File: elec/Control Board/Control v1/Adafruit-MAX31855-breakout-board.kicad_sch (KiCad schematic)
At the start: 17 parts, among them IC1 MAX6675, IC2 LP298XS, J1 1X2-3.5MM

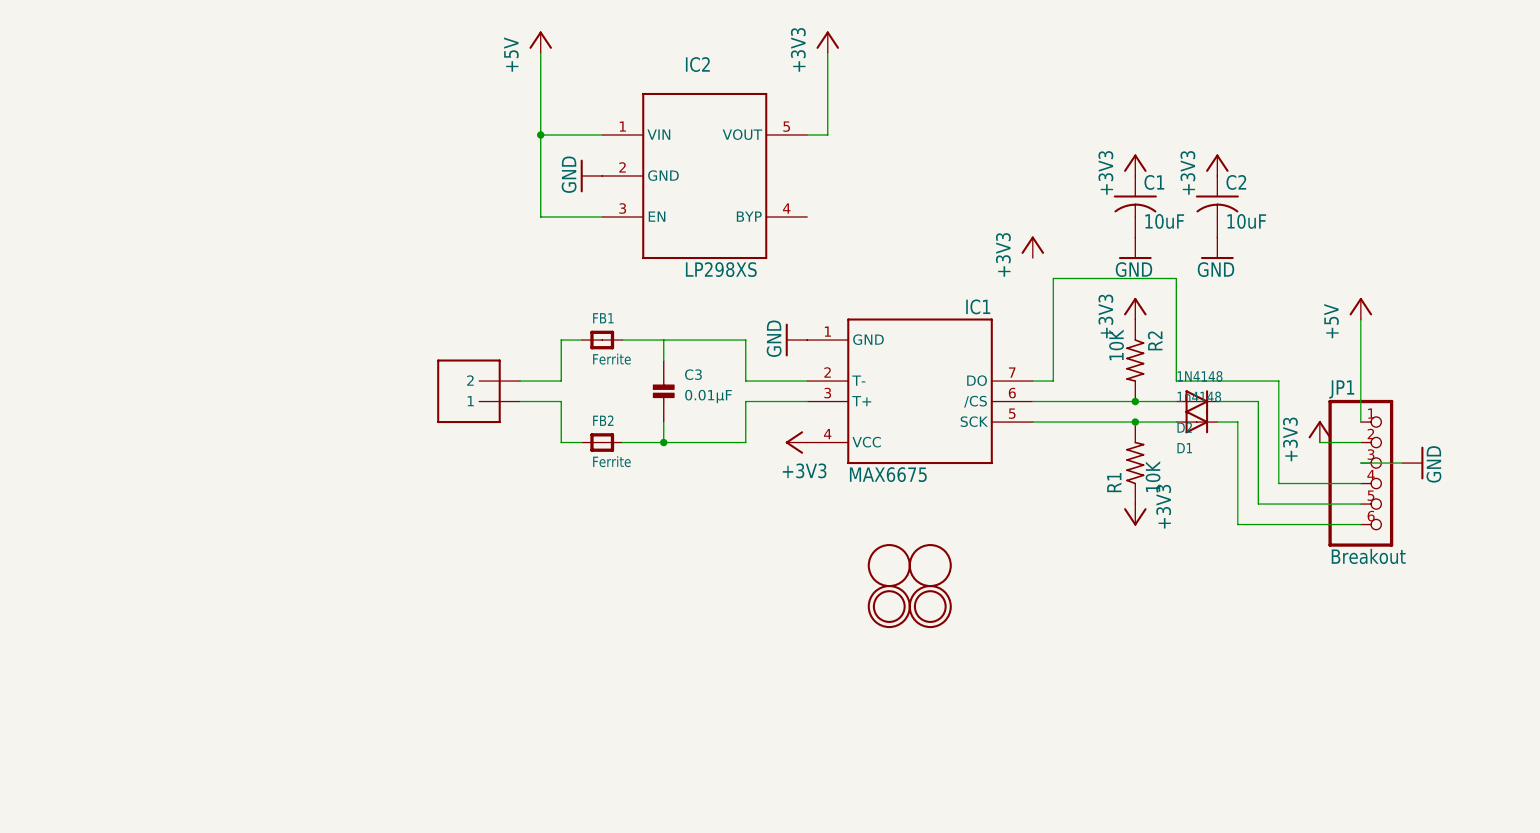
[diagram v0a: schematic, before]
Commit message: added labels for heiarchy sheets, and first pass on basic control interface circuits
Signed-off-by: lokimetasmith <lokimail@gmail.com>
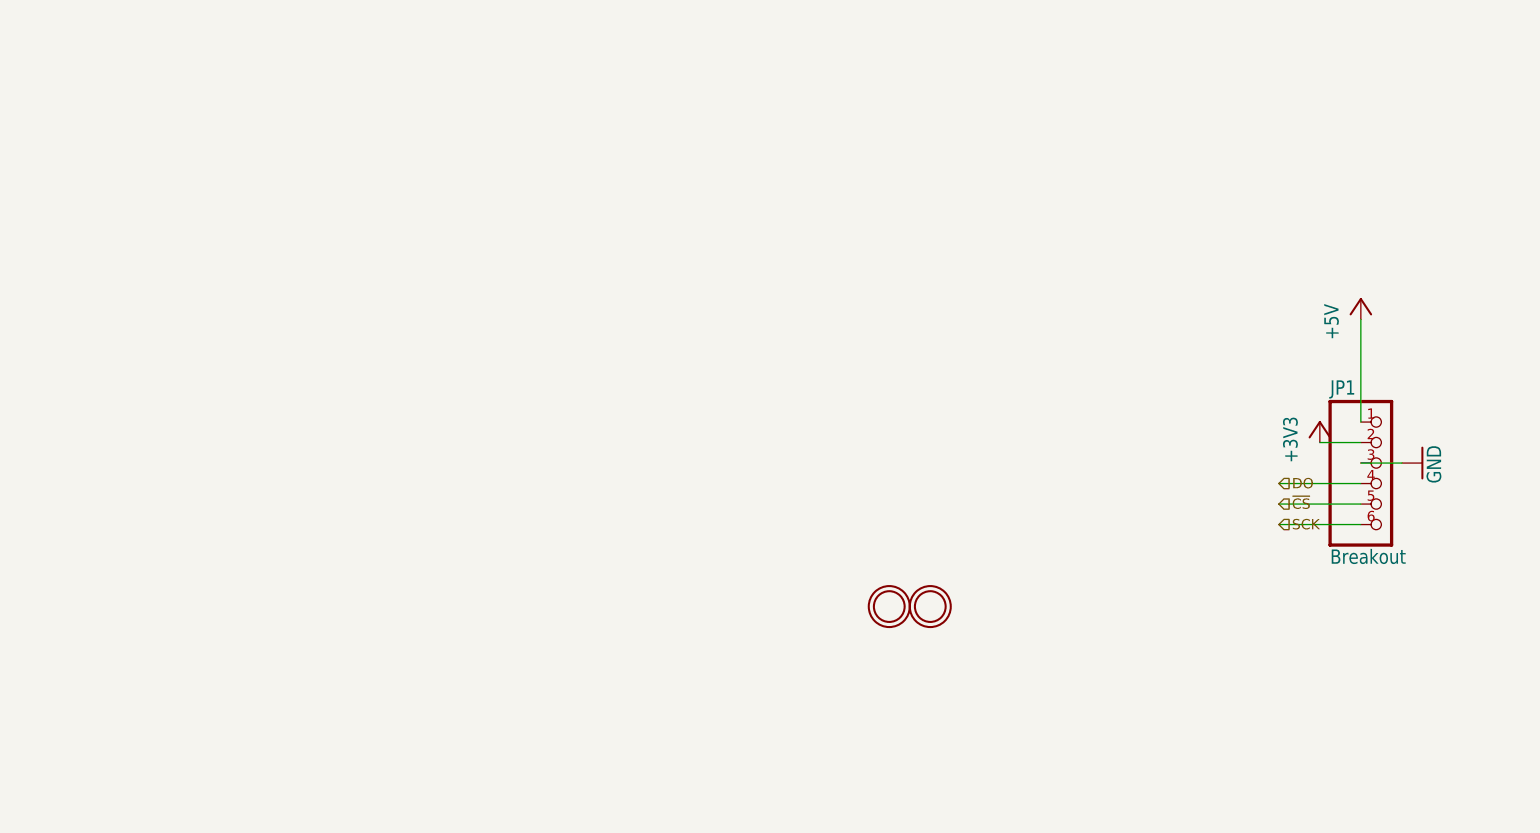
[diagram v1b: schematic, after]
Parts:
- removed C1, C2: 10uF, Control v1:C0805K, symbol Control v1-eagle-import:C-USC0805K
- removed C3: 0.01µF, Control v1:_0805, symbol Control v1-eagle-import:microbuilder_CAP_CERAMIC_0805
- removed D1: 1n4148, Control v1:SOD-323F, symbol Control v1-eagle-import:DIODESOD-323F
- removed D2: 1N4148, Control v1:SOD-323F, symbol Control v1-eagle-import:DIODESOD-323F
- removed FB1, FB2: Ferrite, Control v1:_0805, symbol Control v1-eagle-import:microbuilder_FERRITE_0805
- removed IC1: MAX6675, Control v1:SO08, symbol Control v1-eagle-import:MAX6675
- removed IC2: LP298XS, Control v1:SOT23-5L, symbol Control v1-eagle-import:LP298XS
- removed J1: 1X2-3.5MM, Control v1:1X2-3.5MM, symbol Control v1-eagle-import:1X2-3.5MM
- removed R1, R2: 10K, Control v1:R0805, symbol Control v1-eagle-import:R-US_R0805
- removed U$1, U$2: FIDUCIAL, Control v1:FIDUCIAL_1MM, symbol Control v1-eagle-import:FIDUCIAL
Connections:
- net DO: now reaches JP1.4
- net SCK: now reaches JP1.6
- net ~{CS}: now reaches JP1.5

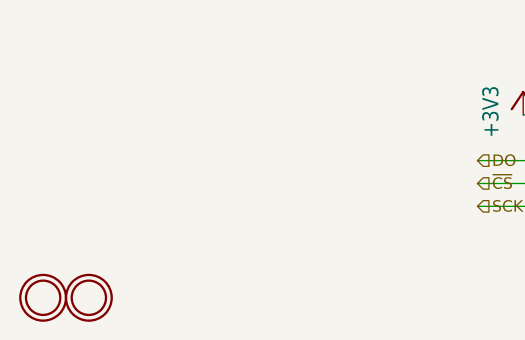
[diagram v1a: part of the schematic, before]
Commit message: Add Lees PublicInvention submodule library. Update Control V1 project and schematic for new library.
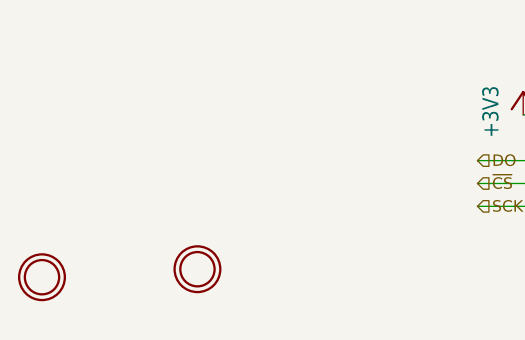
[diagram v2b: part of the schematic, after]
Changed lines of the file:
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@@
     )
   )
-  (symbol (lib_id "Control v1-eagle-import:microbuilder_MOUNTINGHOLE2.0") (at 139.7 139.7 0) (unit 1)
+  (symbol (lib_id "Control v1-eagle-import:microbuilder_MOUNTINGHOLE2.0") (at 139.573 137.414 0) (unit 1)
     (in_bom yes) (on_board yes) (dnp no)
-    (property "Reference" "U$4" (at 139.7 139.7 0)
+    (property "Reference" "U$4" (at 139.573 137.414 0)
       (effects (font (size 1.27 1.27)) hide)
     )
-    (property "Value" "MOUNTINGHOLE2.0" (at 139.7 139.7 0)
+    (property "Value" "MOUNTINGHOLE2.0" (at 139.573 137.414 0)
       (effects (font (size 1.27 1.27)) hide)
     )
-    (property "Footprint" "Control v1:MOUNTINGHOLE_2.0_PLATED" (at 139.7 139.7 0)
+    (property "Footprint" "Control v1:MOUNTINGHOLE_2.0_PLATED" (at 139.573 137.414 0)
       (effects (font (size 1.27 1.27)) hide)
     )
-    (property "Datasheet" "" (at 139.7 139.7 0)
+    (property "Datasheet" "" (at 139.573 137.414 0)
       (effects (font (size 1.27 1.27)) hide)
     )
@@
     )
   )
-  (symbol (lib_id "Control v1-eagle-import:microbuilder_MOUNTINGHOLE2.0") (at 144.78 139.7 0) (unit 1)
+  (symbol (lib_id "Control v1-eagle-import:microbuilder_MOUNTINGHOLE2.0") (at 156.845 136.525 0) (unit 1)
     (in_bom yes) (on_board yes) (dnp no)
-    (property "Reference" "U$5" (at 144.78 139.7 0)
+    (property "Reference" "U$5" (at 156.845 136.525 0)
       (effects (font (size 1.27 1.27)) hide)
     )
-    (property "Value" "MOUNTINGHOLE2.0" (at 144.78 139.7 0)
+    (property "Value" "MOUNTINGHOLE2.0" (at 156.845 136.525 0)
       (effects (font (size 1.27 1.27)) hide)
     )
-    (property "Footprint" "Control v1:MOUNTINGHOLE_2.0_PLATED" (at 144.78 139.7 0)
+    (property "Footprint" "Control v1:MOUNTINGHOLE_2.0_PLATED" (at 156.845 136.525 0)
       (effects (font (size 1.27 1.27)) hide)
     )
-    (property "Datasheet" "" (at 144.78 139.7 0)
+    (property "Datasheet" "" (at 156.845 136.525 0)
       (effects (font (size 1.27 1.27)) hide)
     )

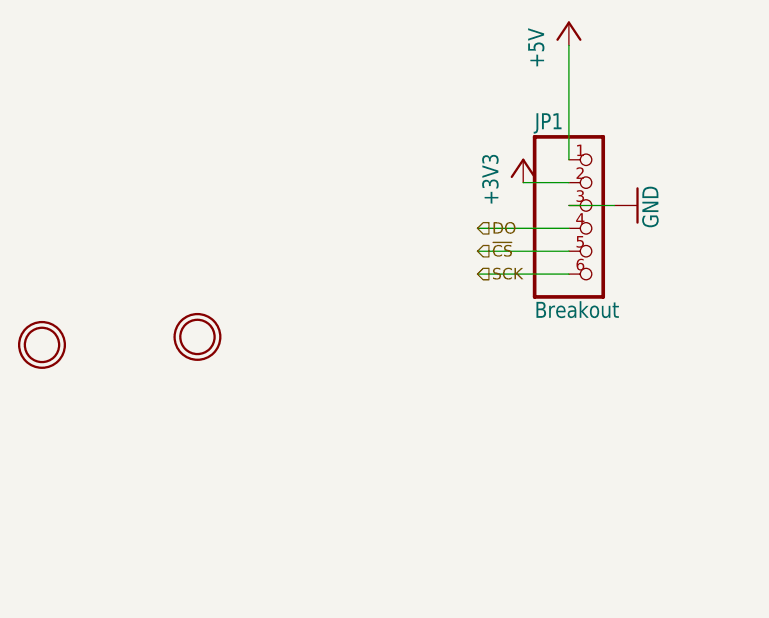
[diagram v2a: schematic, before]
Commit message: Add fan circuits. Add thermocouple interface circuits.
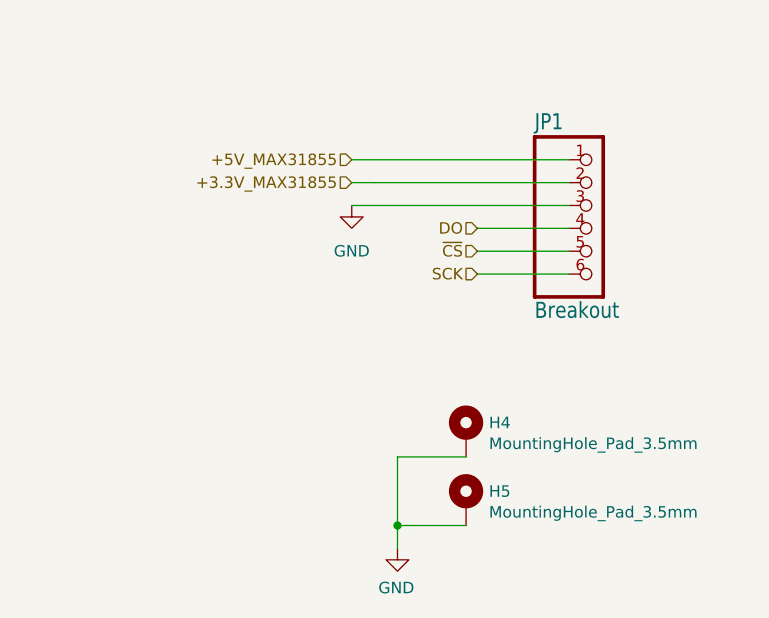
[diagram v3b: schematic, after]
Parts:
- removed U$4, U$5: MOUNTINGHOLE2.0, Control v1:MOUNTINGHOLE_2.0_PLATED, symbol Control v1-eagle-import:microbuilder_MOUNTINGHOLE2.0
- added H4, H5: MountingHole_Pad_3.5mm, GeneralPurposeAlarmDevicePCB:MountingHole_3.5mm_Pad_Via, symbol GPAD_SCH_LIB:MountingHole_Pad_3.5mm
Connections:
- net GND: now also H4.1, H5.1
- net +3V3 renamed +3.3V_MAX31855
- net +5V renamed +5V_MAX31855
